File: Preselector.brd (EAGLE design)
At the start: 183 x 137.8 mm, 266 parts, among them IC58 LMZ31707RVQ, Q2 FDV303N, X1 0733660061, X10 0733660061, X11 0733660061, X12 0733660061, X13 0733660061, X14 0733660061, X15 0733660061, X16 0733660061, X17 0733660061, X18 0733660061, X19 0733660061, X2 0733660061, X20 0733660061, X21 0733660061, X22 0733660061, X23 0733660061, X24 0733660061, X25 0733660061, X26 0733660061, X27 0733660061, X28 0733660061, X29 0733660061, X3 0733660061, X30 0733660061, X31 0733660061, X32 0733660061, X4 0733660061, X5 0733660061, X6 0733660061, X7 0733660061, X8 0733660061, X9 0733660061

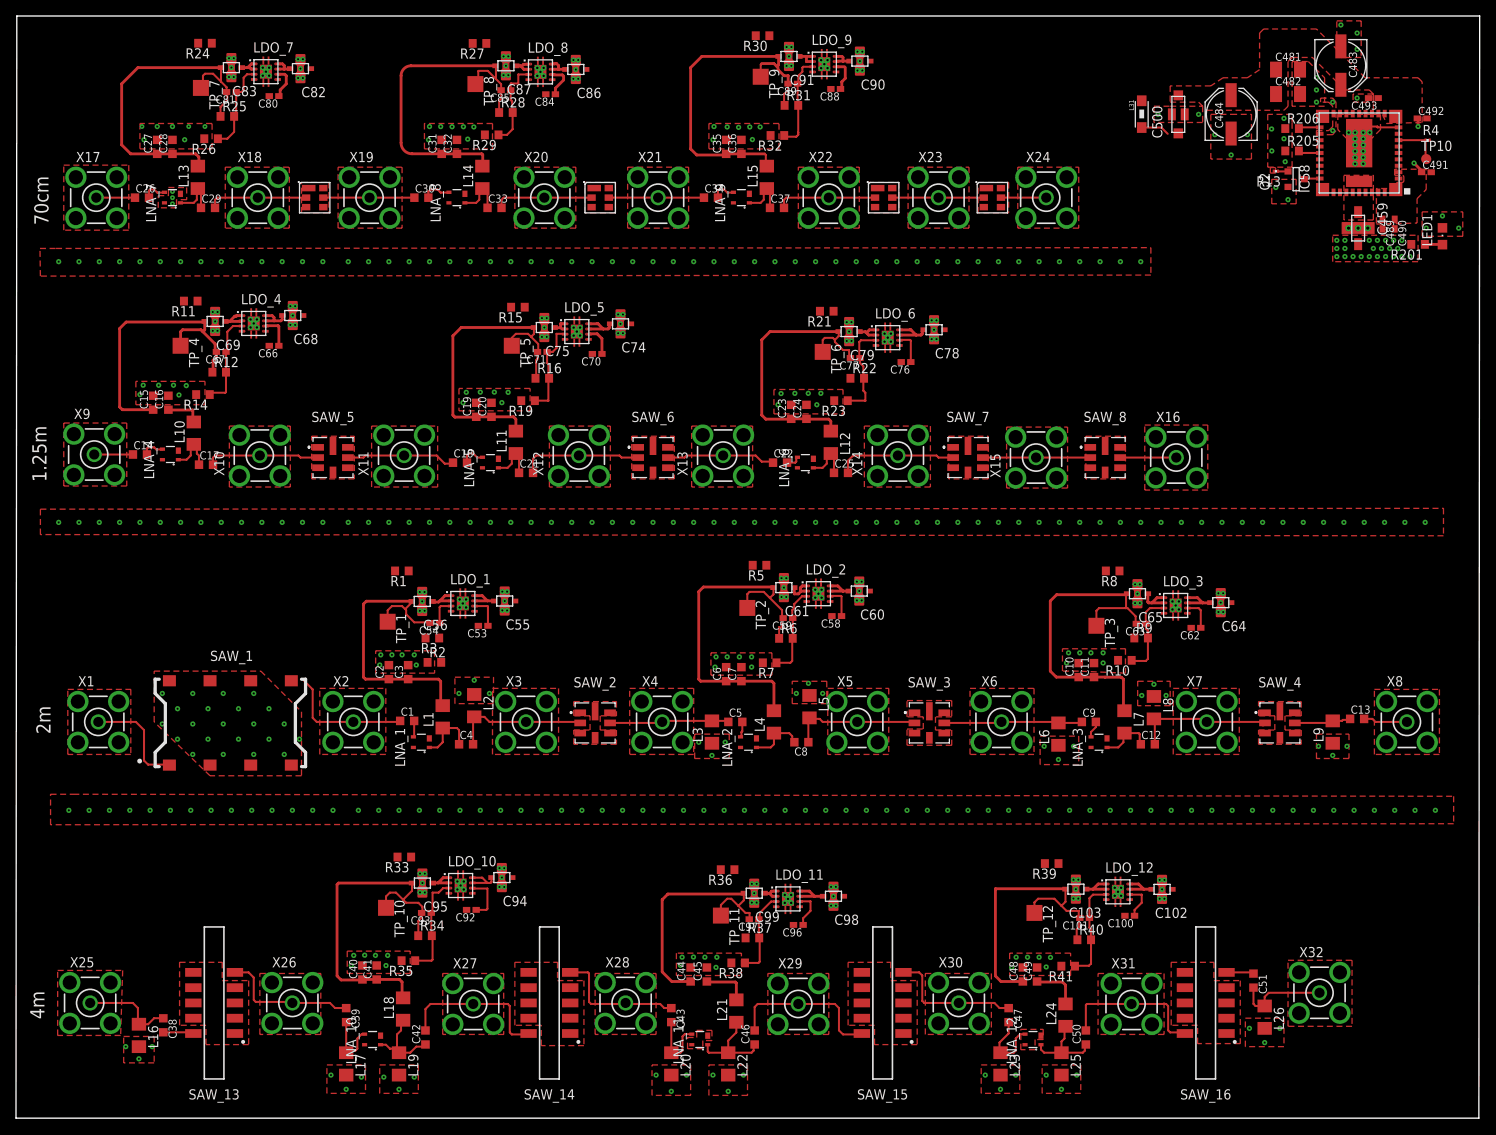
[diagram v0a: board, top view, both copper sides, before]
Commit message: Finished connecting power supply
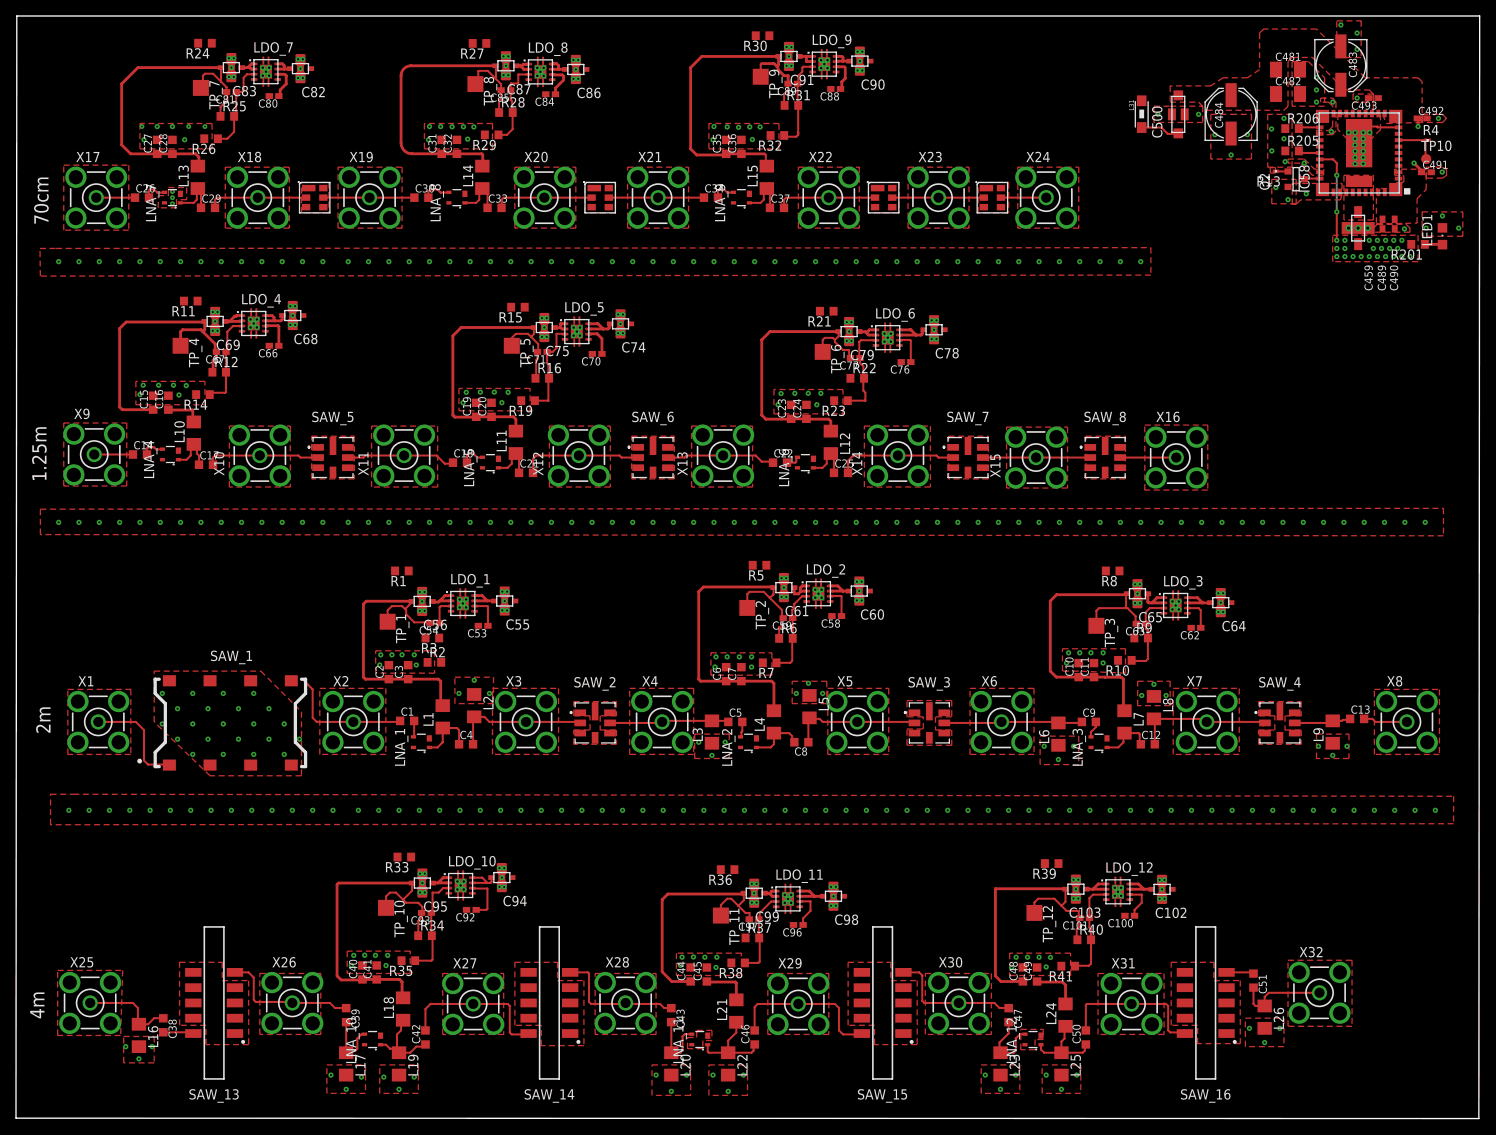
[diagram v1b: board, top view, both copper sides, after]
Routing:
- net +5V3: track 0.00 -> 12.0 mm, vias 23 -> 25
- net N$169: track 3.58 -> 4.92 mm
- removed copper zone on layer 1, net GND2

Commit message: Need 2 polygons for +5v3
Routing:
- net +5V3: vias 25 -> 55
- added copper zone on layer 1, net +5V2
- added copper zone on layer 15, net +5V3
- removed copper zone on layer 15, net PWR
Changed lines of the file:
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@@
 <layers>
 <layer number="1" name="Top" color="4" fill="1" visible="yes" active="yes"/>
-<layer number="2" name="GND" color="1" fill="3" visible="no" active="yes"/>
+<layer number="2" name="GND" color="1" fill="3" visible="yes" active="yes"/>
 <layer number="3" name="Route3" color="4" fill="3" visible="no" active="no"/>
 <layer number="4" name="Route4" color="1" fill="4" visible="no" active="no"/>
@@
 <via x="165.1" y="113.284" extent="1-16" drill="0.254"/>
 <wire x1="165.1" y1="113.284" x2="165.1" y2="109.728" width="0.254" layer="1"/>
+<polygon width="0.254" layer="15">
+<vertex x="0" y="0"/>
+<vertex x="0" y="137.668"/>
+<vertex x="182.88" y="137.668"/>
+<vertex x="182.88" y="0"/>
+</polygon>
+<polygon width="0.1016" layer="1">
+<vertex x="61.468" y="30.607"/>
+<vertex x="62.484" y="31.115"/>
+<vertex x="64.516" y="31.115"/>
+<vertex x="64.516" y="28.956"/>
+<vertex x="62.484" y="28.956"/>
+<vertex x="61.468" y="29.591"/>
+</polygon>
+<via x="64.008" y="30.607" extent="1-16" drill="0.254"/>
+<via x="64.008" y="29.591" extent="1-16" drill="0.254"/>
+<via x="63.246" y="30.099" extent="1-16" drill="0.254"/>
+<polygon width="0.1016" layer="1">
+<vertex x="61.849" y="65.151"/>
+<vertex x="62.865" y="65.659"/>
+<vertex x="64.897" y="65.659"/>
+<vertex x="64.897" y="63.5"/>
+<vertex x="62.865" y="63.5"/>
+<vertex x="61.849" y="64.135"/>
+</polygon>
+<via x="64.389" y="65.151" extent="1-16" drill="0.254"/>
+<via x="64.389" y="64.135" extent="1-16" drill="0.254"/>
+<via x="63.627" y="64.643" extent="1-16" drill="0.254"/>
+<polygon width="0.1016" layer="1">
+<vertex x="102.8954" y="28.2448"/>
+<vertex x="103.9114" y="28.7528"/>
+<vertex x="105.9434" y="28.7528"/>
+<vertex x="105.9434" y="26.5938"/>
+<vertex x="103.9114" y="26.5938"/>
+<vertex x="102.8954" y="27.2288"/>
+</polygon>
+<via x="105.4354" y="28.2448" extent="1-16" drill="0.254"/>
+<via x="105.4354" y="27.2288" extent="1-16" drill="0.254"/>
+<via x="104.6734" y="27.7368" extent="1-16" drill="0.254"/>
+<polygon width="0.1016" layer="1">
+<vertex x="143.9926" y="29.083"/>
+<vertex x="145.0086" y="29.591"/>
+<vertex x="147.0406" y="29.591"/>
+<vertex x="147.0406" y="27.432"/>
+<vertex x="145.0086" y="27.432"/>
+<vertex x="143.9926" y="28.067"/>
+</polygon>
+<via x="146.5326" y="29.083" extent="1-16" drill="0.254"/>
+<via x="146.5326" y="28.067" extent="1-16" drill="0.254"/>
+<via x="145.7706" y="28.575" extent="1-16" drill="0.254"/>
+<polygon width="0.1016" layer="1">
+<vertex x="106.1466" y="66.3956"/>
+<vertex x="107.1626" y="66.9036"/>
+<vertex x="109.1946" y="66.9036"/>
+<vertex x="109.1946" y="64.7446"/>
+<vertex x="107.1626" y="64.7446"/>
+<vertex x="106.1466" y="65.3796"/>
+</polygon>
+<via x="108.6866" y="66.3956" extent="1-16" drill="0.254"/>
+<via x="108.6866" y="65.3796" extent="1-16" drill="0.254"/>
+<via x="107.9246" y="65.8876" extent="1-16" drill="0.254"/>
+<polygon width="0.1016" layer="1">
+<vertex x="151.3332" y="64.9478"/>
+<vertex x="152.3492" y="65.4558"/>
+<vertex x="154.3812" y="65.4558"/>
+<vertex x="154.3812" y="63.2968"/>
+<vertex x="152.3492" y="63.2968"/>
+<vertex x="151.3332" y="63.9318"/>
+</polygon>
+<via x="153.8732" y="64.9478" extent="1-16" drill="0.254"/>
+<via x="153.8732" y="63.9318" extent="1-16" drill="0.254"/>
+<via x="153.1112" y="64.4398" extent="1-16" drill="0.254"/>
+<polygon width="0.1016" layer="1">
+<vertex x="35.3314" y="100.838"/>
+<vertex x="36.3474" y="101.346"/>
+<vertex x="38.3794" y="101.346"/>
+<vertex x="38.3794" y="99.187"/>
+<vertex x="36.3474" y="99.187"/>
+<vertex x="35.3314" y="99.822"/>
+</polygon>
+<via x="37.8714" y="100.838" extent="1-16" drill="0.254"/>
+<via x="37.8714" y="99.822" extent="1-16" drill="0.254"/>
+<via x="37.1094" y="100.33" extent="1-16" drill="0.254"/>
+<polygon width="0.1016" layer="1">
+<vertex x="76.3016" y="99.7966"/>
+<vertex x="77.3176" y="100.3046"/>
+<vertex x="79.3496" y="100.3046"/>
+<vertex x="79.3496" y="98.1456"/>
+<vertex x="77.3176" y="98.1456"/>
+<vertex x="76.3016" y="98.7806"/>
+</polygon>
+<via x="78.8416" y="99.7966" extent="1-16" drill="0.254"/>
+<via x="78.8416" y="98.7806" extent="1-16" drill="0.254"/>
+<via x="78.0796" y="99.2886" extent="1-16" drill="0.254"/>
+<polygon width="0.1016" layer="1">
+<vertex x="115.4938" y="99.06"/>
+<vertex x="116.5098" y="99.568"/>
+<vertex x="118.5418" y="99.568"/>
+<vertex x="118.5418" y="97.409"/>
+<vertex x="116.5098" y="97.409"/>
+<vertex x="115.4938" y="98.044"/>
+</polygon>
+<via x="118.0338" y="99.06" extent="1-16" drill="0.254"/>
+<via x="118.0338" y="98.044" extent="1-16" drill="0.254"/>
+<via x="117.2718" y="98.552" extent="1-16" drill="0.254"/>
+<polygon width="0.1016" layer="1">
+<vertex x="106.2228" y="132.6388"/>
+<vertex x="107.2388" y="133.1468"/>
+<vertex x="109.2708" y="133.1468"/>
+<vertex x="109.2708" y="130.9878"/>
+<vertex x="107.2388" y="130.9878"/>
+<vertex x="106.2228" y="131.6228"/>
+</polygon>
+<via x="108.7628" y="132.6388" extent="1-16" drill="0.254"/>
+<via x="108.7628" y="131.6228" extent="1-16" drill="0.254"/>
+<via x="108.0008" y="132.1308" extent="1-16" drill="0.254"/>
+<wire x1="108.0008" y1="132.1308" x2="106.7862" y2="132.1308" width="0" layer="19" extent="1-1"/>
+<wire x1="49.3894" y1="32.639" x2="62.0314" y2="30.0736" width="0" layer="19" extent="1-1"/>
 <wire x1="94.1696" y1="135.3058" x2="106.7862" y2="132.1308" width="0" layer="19" extent="1-1"/>
+<wire x1="93.7886" y1="69.1134" x2="106.71" y2="65.8876" width="0" layer="19" extent="1-1"/>
+<wire x1="22.694" y1="102.1334" x2="35.8948" y2="100.33" width="0" layer="19" extent="1-1"/>
+<wire x1="63.588" y1="101.3714" x2="76.865" y2="99.2886" width="0" layer="19" extent="1-1"/>
+<wire x1="49.0846" y1="68.4022" x2="62.387" y2="64.643" width="0" layer="19" extent="1-1"/>
+<wire x1="102.196" y1="100.8634" x2="116.0572" y2="98.552" width="0" layer="19" extent="1-1"/>
+<wire x1="89.8008" y1="31.0642" x2="103.4842" y2="27.7368" width="0" layer="19" extent="1-1"/>
+<wire x1="137.9338" y1="68.4022" x2="151.8966" y2="64.4398" width="0" layer="19" extent="1-1"/>
+<wire x1="130.3138" y1="31.8262" x2="144.556" y2="28.6004" width="0" layer="19" extent="1-1"/>
 <wire x1="71.277" y1="131.0894" x2="94.1696" y2="135.3058" width="0" layer="19" extent="1-1"/>
 <wire x1="58.7874" y1="134.3406" x2="71.277" y2="131.0894" width="0" layer="19" extent="1-1"/>
 <wire x1="36.86" y1="131.191" x2="58.7874" y2="134.3406" width="0" layer="19" extent="1-1"/>
 <wire x1="24.472" y1="134.366" x2="36.86" y2="131.191" width="0" layer="19" extent="1-1"/>
-<wire x1="63.588" y1="101.3714" x2="71.277" y2="131.0894" width="0" layer="19" extent="1-1"/>
-<wire x1="76.865" y1="99.2886" x2="63.588" y2="101.3714" width="0" layer="19" extent="1-1"/>
-<wire x1="102.196" y1="100.8634" x2="76.865" y2="99.2886" width="0" layer="19" extent="1-1"/>
-<wire x1="116.0572" y1="98.552" x2="102.196" y2="100.8634" width="0" layer="19" extent="1-1"/>
-<wire x1="35.8948" y1="100.33" x2="63.588" y2="101.3714" width="0" layer="19" extent="1-1"/>
-<wire x1="22.694" y1="102.1334" x2="35.8948" y2="100.33" width="0" layer="19" extent="1-1"/>
-<wire x1="93.7886" y1="69.1134" x2="102.196" y2="100.8634" width="0" layer="19" extent="1-1"/>
-<wire x1="106.71" y1="65.8876" x2="93.7886" y2="69.1134" width="0" layer="19" extent="1-1"/>
-<wire x1="137.9338" y1="68.4022" x2="106.71" y2="65.8876" width="0" layer="19" extent="1-1"/>
-<wire x1="151.8966" y1="64.4398" x2="137.9338" y2="68.4022" width="0" layer="19" extent="1-1"/>
-<wire x1="62.387" y1="64.643" x2="93.7886" y2="69.1134" width="0" layer="19" extent="1-1"/>
-<wire x1="49.0846" y1="68.4022" x2="62.387" y2="64.643" width="0" layer="19" extent="1-1"/>
-<wire x1="49.3894" y1="32.639" x2="62.387" y2="64.643" width="0" layer="19" extent="1-1"/>
-<wire x1="62.0314" y1="30.0736" x2="49.3894" y2="32.639" width="0" layer="19" extent="1-1"/>
-<wire x1="89.8008" y1="31.0642" x2="62.0314" y2="30.0736" width="0" layer="19" extent="1-1"/>
-<wire x1="103.4842" y1="27.7368" x2="89.8008" y2="31.0642" width="0" layer="19" extent="1-1"/>
-<wire x1="130.3138" y1="31.8262" x2="103.4842" y2="27.7368" width="0" layer="19" extent="1-1"/>
-<wire x1="144.556" y1="28.6004" x2="130.3138" y2="31.8262" width="0" layer="19" extent="1-1"/>
-<wire x1="165.1" y1="107.696" x2="151.8966" y2="64.4398" width="0" layer="19" extent="1-1"/>
 </signal>
 <signal name="LNA_4_OUT">
@@
 <wire x1="125.857" y1="17.0828" x2="127.635" y2="17.0828" width="0" layer="19" extent="1-1"/>
 </signal>
-<signal name="PWR">
-<polygon width="0.254" layer="15">
-<vertex x="0" y="0"/>
-<vertex x="0" y="137.668"/>
-<vertex x="182.88" y="137.668"/>
-<vertex x="182.88" y="0"/>
-</polygon>
+<signal name="+5V2">
+<polygon width="0.1016" layer="1">
+<vertex x="69.088" y="33.655"/>
+<vertex x="70.104" y="34.163"/>
+<vertex x="72.136" y="34.163"/>
+<vertex x="72.136" y="32.004"/>
+<vertex x="70.104" y="32.004"/>
+<vertex x="69.088" y="32.639"/>
+</polygon>
+<via x="71.628" y="33.655" extent="1-16" drill="0.254"/>
+<via x="71.628" y="32.639" extent="1-16" drill="0.254"/>
+<via x="70.866" y="33.147" extent="1-16" drill="0.254"/>
 </signal>
 </signals>

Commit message: Fixed Volt Reg power supply and moves Volt Reg names.
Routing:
- net +5V3: track 12.0 -> 0.00 mm, vias 55 -> 50
